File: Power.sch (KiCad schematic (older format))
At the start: 15 parts, among them P4 CONN_01X03, U10 RT9183, U9 TPS799

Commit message: microstrip layed out
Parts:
- C27, C30: footprint SFUSat:C_0402 -> SFUSat:C_1210_HandSoldering
- C29: footprint SFUSat:C_0402 -> SFUSat:C_0603
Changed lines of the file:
@@
 LIBS:valves
 LIBS:SFUSat
+LIBS:SFUSat-Radio-cache
 EELAYER 25 0
 EELAYER END
@@
 F 0 "C27" H 5725 2700 50  0000 L CNN
 F 1 "10uF" H 5725 2500 50  0000 L CNN
-F 2 "SFUSat:C_0402" H 5738 2450 50  0001 C CNN
+F 2 "SFUSat:C_1210_HandSoldering" H 5738 2450 50  0001 C CNN
 F 3 "" H 5700 2600 50  0000 C CNN
 	1    5700 2600
@@
 $EndComp
 $Comp
-L GND #PWR041
+L GND #PWR046
 U 1 1 58770941
 P 6900 2800
-F 0 "#PWR041" H 6900 2550 50  0001 C CNN
+F 0 "#PWR046" H 6900 2550 50  0001 C CNN
 F 1 "GND" H 6900 2650 50  0000 C CNN
 F 2 "" H 6900 2800 50  0000 C CNN
@@
 F 0 "C30" H 8075 2700 50  0000 L CNN
 F 1 "10uF" H 8075 2500 50  0000 L CNN
-F 2 "SFUSat:C_0402" H 8088 2450 50  0001 C CNN
+F 2 "SFUSat:C_1210_HandSoldering" H 8088 2450 50  0001 C CNN
 F 3 "" H 8050 2600 50  0000 C CNN
 	1    8050 2600
@@
 $EndComp
 $Comp
-L GND #PWR042
+L GND #PWR047
 U 1 1 58770B93
 P 8050 2750
-F 0 "#PWR042" H 8050 2500 50  0001 C CNN
+F 0 "#PWR047" H 8050 2500 50  0001 C CNN
 F 1 "GND" H 8050 2600 50  0000 C CNN
 F 2 "" H 8050 2750 50  0000 C CNN
@@
 $EndComp
 $Comp
-L GND #PWR043
+L GND #PWR048
 U 1 1 58770BD7
 P 7650 2750
-F 0 "#PWR043" H 7650 2500 50  0001 C CNN
+F 0 "#PWR048" H 7650 2500 50  0001 C CNN
 F 1 "GND" H 7650 2600 50  0000 C CNN
 F 2 "" H 7650 2750 50  0000 C CNN
@@
 $EndComp
 $Comp
-L GND #PWR044
+L GND #PWR049
 U 1 1 58770CCB
 P 5700 2750
-F 0 "#PWR044" H 5700 2500 50  0001 C CNN
+F 0 "#PWR049" H 5700 2500 50  0001 C CNN
 F 1 "GND" H 5700 2600 50  0000 C CNN
 F 2 "" H 5700 2750 50  0000 C CNN
@@
 $EndComp
 $Comp
-L GND #PWR045
+L GND #PWR050
 U 1 1 58770CE7
 P 5400 2750
-F 0 "#PWR045" H 5400 2500 50  0001 C CNN
+F 0 "#PWR050" H 5400 2500 50  0001 C CNN
 F 1 "GND" H 5400 2600 50  0000 C CNN
 F 2 "" H 5400 2750 50  0000 C CNN
@@
 $EndComp
 $Comp
-L GND #PWR046
+L GND #PWR051
 U 1 1 5879D9E2
 P 6350 4000
-F 0 "#PWR046" H 6350 3750 50  0001 C CNN
+F 0 "#PWR051" H 6350 3750 50  0001 C CNN
 F 1 "GND" H 6350 3850 50  0000 C CNN
 F 2 "" H 6350 4000 50  0000 C CNN
@@
 $EndComp
 $Comp
-L GND #PWR047
+L GND #PWR052
 U 1 1 5879DA04
 P 7150 4000
-F 0 "#PWR047" H 7150 3750 50  0001 C CNN
+F 0 "#PWR052" H 7150 3750 50  0001 C CNN
 F 1 "GND" H 7150 3850 50  0000 C CNN
 F 2 "" H 7150 4000 50  0000 C CNN
@@
 $EndComp
 $Comp
-L GND #PWR048
+L GND #PWR053
 U 1 1 5879DA26
 P 6950 4000
-F 0 "#PWR048" H 6950 3750 50  0001 C CNN
+F 0 "#PWR053" H 6950 3750 50  0001 C CNN
 F 1 "GND" H 6950 3850 50  0000 C CNN
 F 2 "" H 6950 4000 50  0000 C CNN
@@
 F 0 "C29" H 7175 3950 50  0000 L CNN
 F 1 "2.2uF" H 7175 3750 50  0000 L CNN
-F 2 "SFUSat:C_0402" H 7188 3700 50  0001 C CNN
+F 2 "SFUSat:C_0603" H 7188 3700 50  0001 C CNN
 F 3 "" H 7150 3850 50  0000 C CNN
 	1    7150 3850
@@
 $EndComp
 $Comp
-L GND #PWR049
+L GND #PWR054
 U 1 1 5879E264
 P 5400 4000
-F 0 "#PWR049" H 5400 3750 50  0001 C CNN
+F 0 "#PWR054" H 5400 3750 50  0001 C CNN
 F 1 "GND" H 5400 3850 50  0000 C CNN
 F 2 "" H 5400 4000 50  0000 C CNN

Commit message: layout complete
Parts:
- U9: footprint SFUSat:SOT-363 -> SFUSat:PDSO-G5
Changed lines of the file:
@@
 $EndComp
 $Comp
-L GND #PWR046
+L GND #PWR042
 U 1 1 58770941
 P 6900 2800
-F 0 "#PWR046" H 6900 2550 50  0001 C CNN
+F 0 "#PWR042" H 6900 2550 50  0001 C CNN
 F 1 "GND" H 6900 2650 50  0000 C CNN
 F 2 "" H 6900 2800 50  0000 C CNN
@@
 $EndComp
 $Comp
-L GND #PWR047
+L GND #PWR043
 U 1 1 58770B93
 P 8050 2750
-F 0 "#PWR047" H 8050 2500 50  0001 C CNN
+F 0 "#PWR043" H 8050 2500 50  0001 C CNN
 F 1 "GND" H 8050 2600 50  0000 C CNN
 F 2 "" H 8050 2750 50  0000 C CNN
@@
 $EndComp
 $Comp
-L GND #PWR048
+L GND #PWR044
 U 1 1 58770BD7
 P 7650 2750
-F 0 "#PWR048" H 7650 2500 50  0001 C CNN
+F 0 "#PWR044" H 7650 2500 50  0001 C CNN
 F 1 "GND" H 7650 2600 50  0000 C CNN
 F 2 "" H 7650 2750 50  0000 C CNN
@@
 $EndComp
 $Comp
-L GND #PWR049
+L GND #PWR045
 U 1 1 58770CCB
 P 5700 2750
-F 0 "#PWR049" H 5700 2500 50  0001 C CNN
+F 0 "#PWR045" H 5700 2500 50  0001 C CNN
 F 1 "GND" H 5700 2600 50  0000 C CNN
 F 2 "" H 5700 2750 50  0000 C CNN
@@
 $EndComp
 $Comp
-L GND #PWR050
+L GND #PWR046
 U 1 1 58770CE7
 P 5400 2750
-F 0 "#PWR050" H 5400 2500 50  0001 C CNN
+F 0 "#PWR046" H 5400 2500 50  0001 C CNN
 F 1 "GND" H 5400 2600 50  0000 C CNN
 F 2 "" H 5400 2750 50  0000 C CNN
@@
 F 0 "U9" H 6600 3700 60  0000 C CNN
 F 1 "TPS799" H 6350 3450 60  0000 C CNN
-F 2 "SFUSat:SOT-363" H 6350 3450 60  0001 C CNN
+F 2 "SFUSat:PDSO-G5" H 6350 3450 60  0001 C CNN
 F 3 "" H 6350 3450 60  0001 C CNN
 	1    6350 3450
@@
 $EndComp
 $Comp
-L GND #PWR051
+L GND #PWR047
 U 1 1 5879D9E2
 P 6350 4000
-F 0 "#PWR051" H 6350 3750 50  0001 C CNN
+F 0 "#PWR047" H 6350 3750 50  0001 C CNN
 F 1 "GND" H 6350 3850 50  0000 C CNN
 F 2 "" H 6350 4000 50  0000 C CNN
@@
 $EndComp
 $Comp
-L GND #PWR052
+L GND #PWR048
 U 1 1 5879DA04
 P 7150 4000
-F 0 "#PWR052" H 7150 3750 50  0001 C CNN
+F 0 "#PWR048" H 7150 3750 50  0001 C CNN
 F 1 "GND" H 7150 3850 50  0000 C CNN
 F 2 "" H 7150 4000 50  0000 C CNN
@@
 $EndComp
 $Comp
-L GND #PWR053
+L GND #PWR049
 U 1 1 5879DA26
 P 6950 4000
-F 0 "#PWR053" H 6950 3750 50  0001 C CNN
+F 0 "#PWR049" H 6950 3750 50  0001 C CNN
 F 1 "GND" H 6950 3850 50  0000 C CNN
 F 2 "" H 6950 4000 50  0000 C CNN
@@
 $EndComp
 $Comp
-L GND #PWR054
+L GND #PWR050
 U 1 1 5879E264
 P 5400 4000
-F 0 "#PWR054" H 5400 3750 50  0001 C CNN
+F 0 "#PWR050" H 5400 3750 50  0001 C CNN
 F 1 "GND" H 5400 3850 50  0000 C CNN
 F 2 "" H 5400 4000 50  0000 C CNN

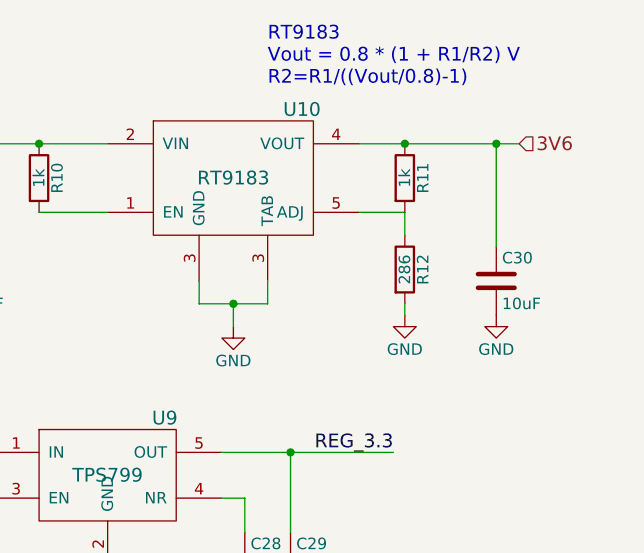
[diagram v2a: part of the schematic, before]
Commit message: Changed R12 and R13 to 287 ohms
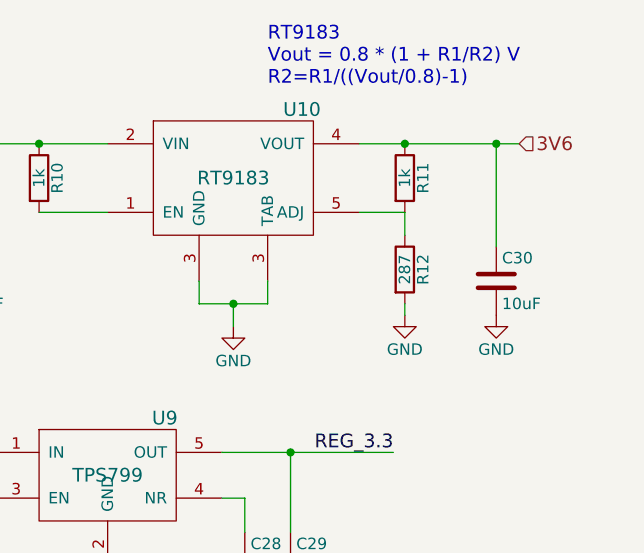
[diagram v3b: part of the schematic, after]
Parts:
- R12: value 286 -> 287
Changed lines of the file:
@@
 P 7650 2550
 F 0 "R12" V 7730 2550 50  0000 C CNN
-F 1 "286" V 7650 2550 50  0000 C CNN
+F 1 "287" V 7650 2550 50  0000 C CNN
 F 2 "SFUSat:R_0402" V 7580 2550 50  0001 C CNN
 F 3 "" H 7650 2550 50  0000 C CNN

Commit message: added TVS to TP
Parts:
- added D? (x2): PESD5Zx, symbol PESD5Zx
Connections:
- wire segments 27 -> 32
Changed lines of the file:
@@
 Connection ~ 5550 3350
 Connection ~ 5400 3350
+$Comp
+L PESD5Zx D?
+U 1 1 593C9E03
+P 2850 5300
+F 0 "D?" H 2950 5100 60  0000 C CNN
+F 1 "PESD5Zx" H 2600 5400 60  0000 C CNN
+F 2 "" H 2850 5300 60  0001 C CNN
+F 3 "" H 2850 5300 60  0001 C CNN
+	1    2850 5300
+	1    0    0    -1
+$EndComp
+$Comp
+L PESD5Zx D?
+U 1 1 593CA01C
+P 3075 5300
+F 0 "D?" H 3175 5100 60  0000 C CNN
+F 1 "PESD5Zx" H 2825 5400 60  0000 C CNN
+F 2 "" H 3075 5300 60  0001 C CNN
+F 3 "" H 3075 5300 60  0001 C CNN
+	1    3075 5300
+	1    0    0    -1
+$EndComp
+$Comp
+L GND #PWR?
+U 1 1 593CA10C
+P 2850 5650
+F 0 "#PWR?" H 2850 5400 50  0001 C CNN
+F 1 "GND" H 2850 5500 50  0000 C CNN
+F 2 "" H 2850 5650 50  0001 C CNN
+F 3 "" H 2850 5650 50  0001 C CNN
+	1    2850 5650
+	1    0    0    -1
+$EndComp
+$Comp
+L GND #PWR?
+U 1 1 593CA241
+P 3075 5650
+F 0 "#PWR?" H 3075 5400 50  0001 C CNN
+F 1 "GND" H 3075 5500 50  0000 C CNN
+F 2 "" H 3075 5650 50  0001 C CNN
+F 3 "" H 3075 5650 50  0001 C CNN
+	1    3075 5650
+	1    0    0    -1
+$EndComp
+Wire Wire Line
+	3075 5600 3075 5650
+Wire Wire Line
+	2850 5650 2850 5600
+Wire Wire Line
+	2850 5000 2850 4600
+Connection ~ 2850 4600
+Wire Wire Line
+	3075 5000 3075 4800
+Wire Wire Line
+	3075 4800 3025 4800
+Connection ~ 3025 4800
 $EndSCHEMATC

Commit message: IC->passive pad 30mil clearance
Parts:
- D6, D7: renamed from D?; footprint (none) -> SFUSat:PESD57zx
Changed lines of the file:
@@
 $EndComp
 $Comp
-L GND #PWR044
+L GND #PWR045
 U 1 1 58770941
 P 6900 2800
-F 0 "#PWR044" H 6900 2550 50  0001 C CNN
+F 0 "#PWR045" H 6900 2550 50  0001 C CNN
 F 1 "GND" H 6900 2650 50  0000 C CNN
 F 2 "" H 6900 2800 50  0000 C CNN
@@
 $EndComp
 $Comp
-L GND #PWR045
+L GND #PWR046
 U 1 1 58770B93
 P 8050 2750
-F 0 "#PWR045" H 8050 2500 50  0001 C CNN
+F 0 "#PWR046" H 8050 2500 50  0001 C CNN
 F 1 "GND" H 8050 2600 50  0000 C CNN
 F 2 "" H 8050 2750 50  0000 C CNN
@@
 $EndComp
 $Comp
-L GND #PWR046
+L GND #PWR047
 U 1 1 58770BD7
 P 7650 2750
-F 0 "#PWR046" H 7650 2500 50  0001 C CNN
+F 0 "#PWR047" H 7650 2500 50  0001 C CNN
 F 1 "GND" H 7650 2600 50  0000 C CNN
 F 2 "" H 7650 2750 50  0000 C CNN
@@
 $EndComp
 $Comp
-L GND #PWR047
+L GND #PWR048
 U 1 1 58770CCB
 P 5700 2750
-F 0 "#PWR047" H 5700 2500 50  0001 C CNN
+F 0 "#PWR048" H 5700 2500 50  0001 C CNN
 F 1 "GND" H 5700 2600 50  0000 C CNN
 F 2 "" H 5700 2750 50  0000 C CNN
@@
 $EndComp
 $Comp
-L GND #PWR048
+L GND #PWR049
 U 1 1 58770CE7
 P 5400 2750
-F 0 "#PWR048" H 5400 2500 50  0001 C CNN
+F 0 "#PWR049" H 5400 2500 50  0001 C CNN
 F 1 "GND" H 5400 2600 50  0000 C CNN
 F 2 "" H 5400 2750 50  0000 C CNN
@@
 $EndComp
 $Comp
-L GND #PWR049
+L GND #PWR050
 U 1 1 5879D9E2
 P 6350 4000
-F 0 "#PWR049" H 6350 3750 50  0001 C CNN
+F 0 "#PWR050" H 6350 3750 50  0001 C CNN
 F 1 "GND" H 6350 3850 50  0000 C CNN
 F 2 "" H 6350 4000 50  0000 C CNN
@@
 $EndComp
 $Comp
-L GND #PWR050
+L GND #PWR051
 U 1 1 5879DA04
 P 7150 4000
-F 0 "#PWR050" H 7150 3750 50  0001 C CNN
+F 0 "#PWR051" H 7150 3750 50  0001 C CNN
 F 1 "GND" H 7150 3850 50  0000 C CNN
 F 2 "" H 7150 4000 50  0000 C CNN
@@
 $EndComp
 $Comp
-L GND #PWR051
+L GND #PWR052
 U 1 1 5879DA26
 P 6950 4000
-F 0 "#PWR051" H 6950 3750 50  0001 C CNN
+F 0 "#PWR052" H 6950 3750 50  0001 C CNN
 F 1 "GND" H 6950 3850 50  0000 C CNN
 F 2 "" H 6950 4000 50  0000 C CNN
@@
 $EndComp
 $Comp
-L GND #PWR052
+L GND #PWR053
 U 1 1 5879E264
 P 5400 4000
-F 0 "#PWR052" H 5400 3750 50  0001 C CNN
+F 0 "#PWR053" H 5400 3750 50  0001 C CNN
 F 1 "GND" H 5400 3850 50  0000 C CNN
 F 2 "" H 5400 4000 50  0000 C CNN
@@
 Connection ~ 5400 3350
 $Comp
-L PESD5Zx D?
+L PESD5Zx D6
 U 1 1 593C9E03
 P 2850 5300
-F 0 "D?" H 2950 5100 60  0000 C CNN
+F 0 "D6" H 2950 5100 60  0000 C CNN
 F 1 "PESD5Zx" H 2600 5400 60  0000 C CNN
-F 2 "" H 2850 5300 60  0001 C CNN
+F 2 "SFUSat:PESD57zx" H 2850 5300 60  0001 C CNN
 F 3 "" H 2850 5300 60  0001 C CNN
 	1    2850 5300
@@
 $EndComp
 $Comp
-L PESD5Zx D?
+L PESD5Zx D7
 U 1 1 593CA01C
 P 3075 5300
-F 0 "D?" H 3175 5100 60  0000 C CNN
+F 0 "D7" H 3175 5100 60  0000 C CNN
 F 1 "PESD5Zx" H 2825 5400 60  0000 C CNN
-F 2 "" H 3075 5300 60  0001 C CNN
+F 2 "SFUSat:PESD57zx" H 3075 5300 60  0001 C CNN
 F 3 "" H 3075 5300 60  0001 C CNN
 	1    3075 5300
@@
 $EndComp
 $Comp
-L GND #PWR?
+L GND #PWR054
 U 1 1 593CA10C
 P 2850 5650
-F 0 "#PWR?" H 2850 5400 50  0001 C CNN
+F 0 "#PWR054" H 2850 5400 50  0001 C CNN
 F 1 "GND" H 2850 5500 50  0000 C CNN
 F 2 "" H 2850 5650 50  0001 C CNN
@@
 $EndComp
 $Comp
-L GND #PWR?
+L GND #PWR055
 U 1 1 593CA241
 P 3075 5650
-F 0 "#PWR?" H 3075 5400 50  0001 C CNN
+F 0 "#PWR055" H 3075 5400 50  0001 C CNN
 F 1 "GND" H 3075 5500 50  0000 C CNN
 F 2 "" H 3075 5650 50  0001 C CNN

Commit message: added TVS on op_3v3
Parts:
- added D8: PESD5Zx, SFUSat:PESD57zx, symbol PESD5Zx
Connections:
- wire segments 32 -> 35
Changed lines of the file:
@@
 	3075 4800 3025 4800
 Connection ~ 3025 4800
+Text HLabel 3900 4575 0    60   Input ~ 0
+OP_3V3
+$Comp
+L PESD5Zx D8
+U 1 1 593DEE02
+P 4050 4975
+F 0 "D8" H 4150 4775 60  0000 C CNN
+F 1 "PESD5Zx" H 3800 5075 60  0000 C CNN
+F 2 "SFUSat:PESD57zx" H 4050 4975 60  0001 C CNN
+F 3 "" H 4050 4975 60  0001 C CNN
+	1    4050 4975
+	1    0    0    -1
+$EndComp
+$Comp
+L GND #PWR056
+U 1 1 593DEF02
+P 4050 5350
+F 0 "#PWR056" H 4050 5100 50  0001 C CNN
+F 1 "GND" H 4050 5200 50  0000 C CNN
+F 2 "" H 4050 5350 50  0001 C CNN
+F 3 "" H 4050 5350 50  0001 C CNN
+	1    4050 5350
+	1    0    0    -1
+$EndComp
+Wire Wire Line
+	3900 4575 4050 4575
+Wire Wire Line
+	4050 4575 4050 4675
+Wire Wire Line
+	4050 5275 4050 5350
 $EndSCHEMATC
